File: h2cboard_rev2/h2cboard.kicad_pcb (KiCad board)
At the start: 4 copper layers, 40 x 27 mm, 19 parts, among them J1 HDMI_A, J2 SJ1-3525NG, J3 SCART-M, SW1 0S102011MS2QN1, U1 NX3303X, U2 ATtiny1604-SS

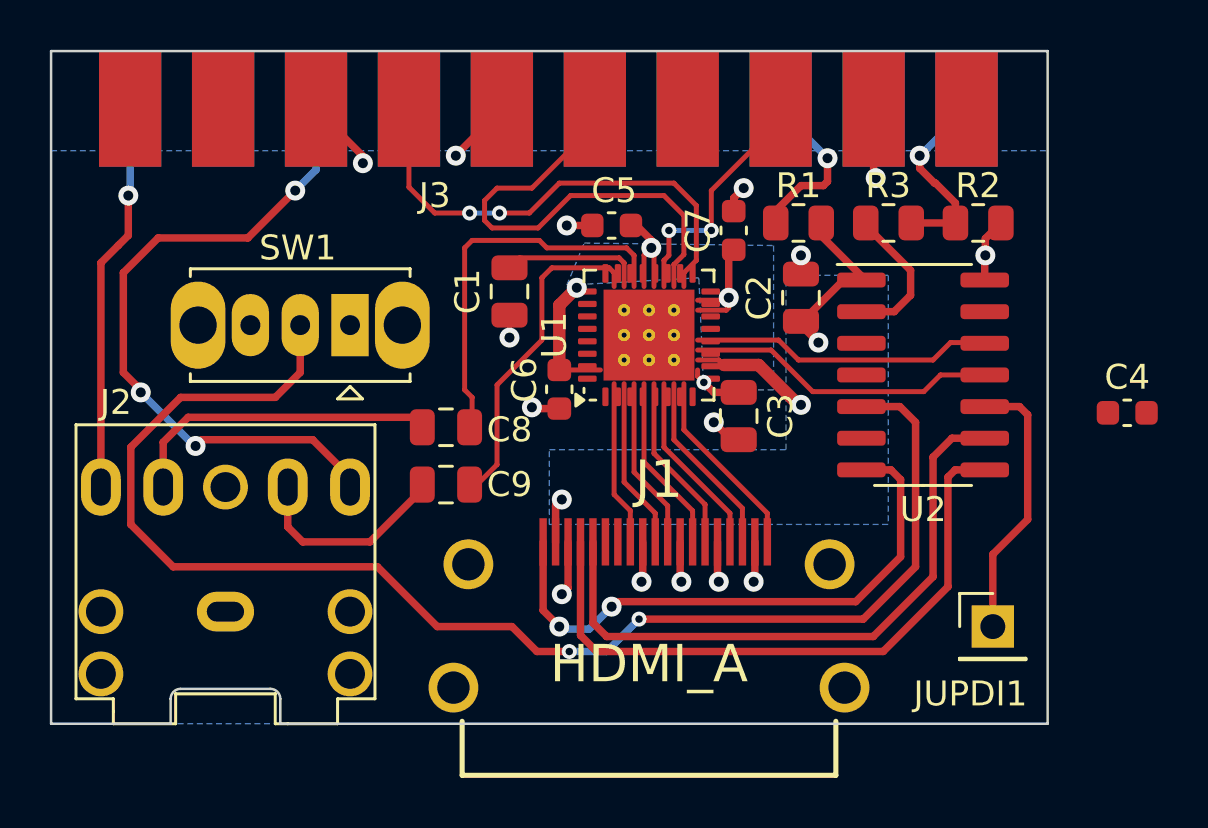
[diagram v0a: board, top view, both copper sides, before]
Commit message: New PCB layout for rev.2
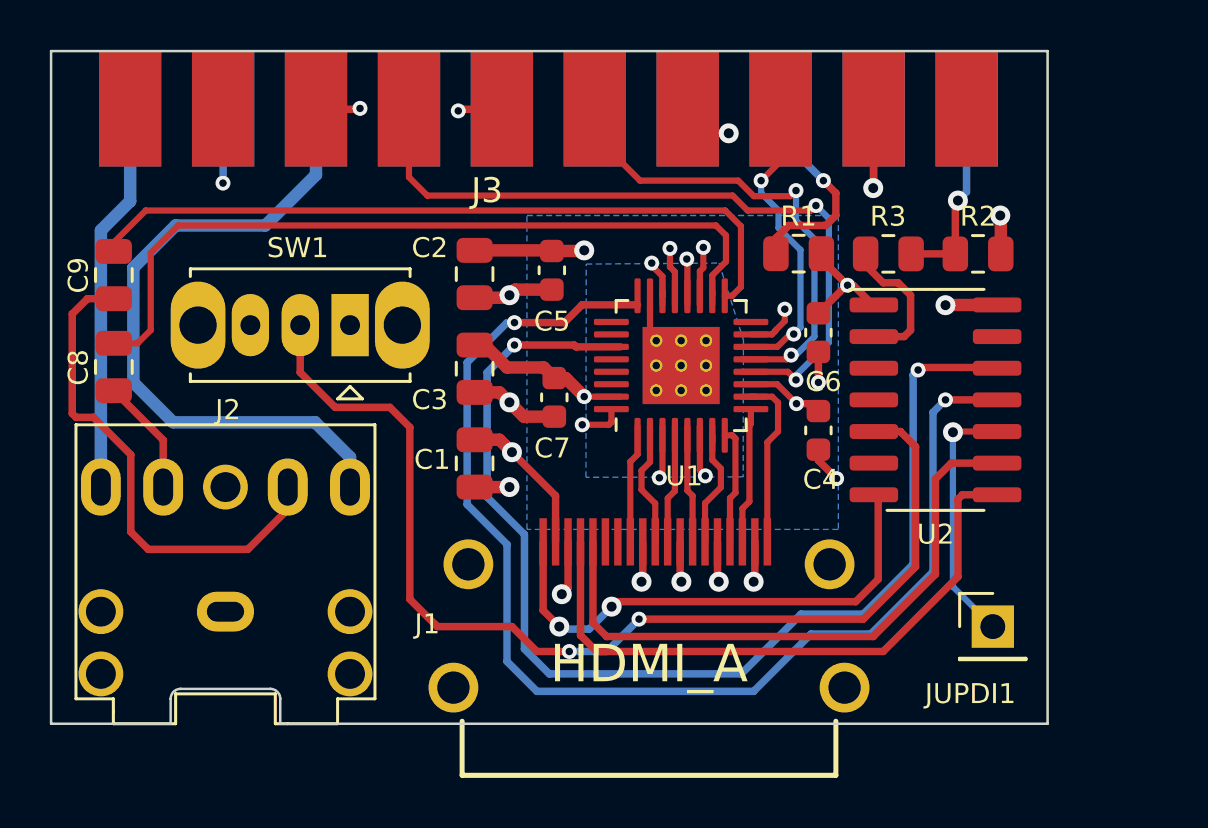
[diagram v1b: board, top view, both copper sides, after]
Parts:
- U1: footprint Package_DFN_QFN:QFN-32-1EP_5x5mm_P0.5mm_EP3.65x3.65mm_ThermalVias -> footprints:QFN-32-1EP_5x5mm_P0.5mm_EP3.1x3.1mm_ThermalVias
- moved C9 15.8 mm to (128.5, 81.0), turned to -90 degrees
- moved C8 13.5 mm to (128.5, 84.7), turned to -90 degrees
- moved C2 13.1 mm to (143.0, 81.0), turned to -90 degrees
- moved C4 12.4 mm to (156.8, 87.2), turned to -90 degrees
- moved C3 10.8 mm to (143.0, 84.8)
- moved C6 10.6 mm to (156.8, 83.3)
- moved C7 9.84 mm to (146.2, 85.9), turned to -90 degrees
- moved C1 7.04 mm to (143.0, 88.5), turned to -90 degrees
- moved C5 3.00 mm to (146.1, 80.8), turned to -90 degrees
- moved U1 1.78 mm to (151.3, 84.6)
- moved R2 1.24 mm to (163.2, 80.1)
- moved R3 1.24 mm to (159.6, 80.1)
- moved R1 1.23 mm to (156.0, 80.1)
- moved U2 1.12 mm to (161.5, 86.0)
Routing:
- net /VSYNC: track 12.5 -> 49.2 mm, vias 0 -> 2
- net /HSYNC: track 12.2 -> 46.5 mm, vias 0 -> 2
- net /AUD_R: track 0.00 -> 31.7 mm
- net /AUD_L: track 0.00 -> 29.6 mm
- net Net-(C8-Pad1): track 15.8 -> 0.00 mm
- net Net-(C9-Pad1): track 13.4 -> 0.00 mm
- net /60Hz: track 56.3 -> 43.4 mm
- net Net-(C9-Pad2): track 8.32 -> 20.2 mm
- net +1V2: track 0.00 -> 10.7 mm, vias 0 -> 3
- net GND: track 30.7 -> 41.1 mm, vias 14 -> 17
- net /B: track 19.4 -> 29.8 mm
- net Net-(C8-Pad2): track 12.8 -> 4.69 mm
- net Net-(J1-Pad1): track 7.78 -> 0.00 mm
- net Net-(J1-Pad4): track 7.49 -> 0.00 mm
- net Net-(J1-Pad6): track 7.24 -> 0.00 mm
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- added copper zone on B.Cu, net +1V2
- added copper zone on In1.Cu, net +5V
- added copper zone on In2.Cu, net GND
- removed copper zone on B.Cu, net +5V
- removed copper zone on B.Cu, net GND
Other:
- board text added: "HDMI2SCART Rev. 2"
- board text removed: "HDMI2SCART Rev 1 © 2024 c0pperdragon"
